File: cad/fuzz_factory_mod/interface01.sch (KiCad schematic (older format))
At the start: 26 parts

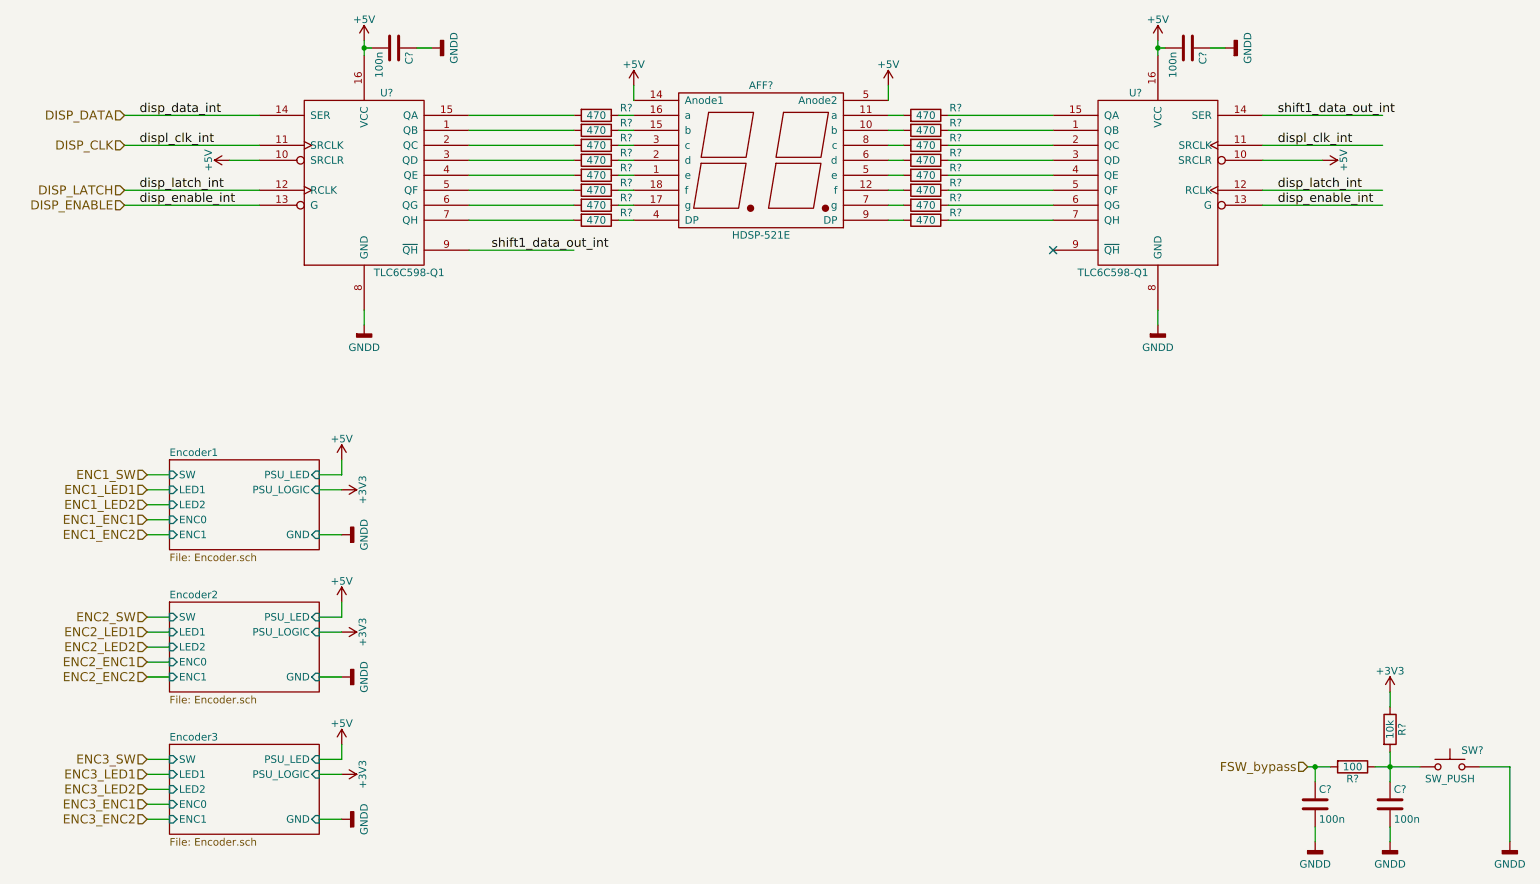
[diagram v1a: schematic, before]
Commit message: Continued schematic.
Modified fuuz_factory circuit : use of matched transistor pairs.
Added USB interface, through FT230X and direct to MCU.
Associated footprints, except for XTAL and trimmers.
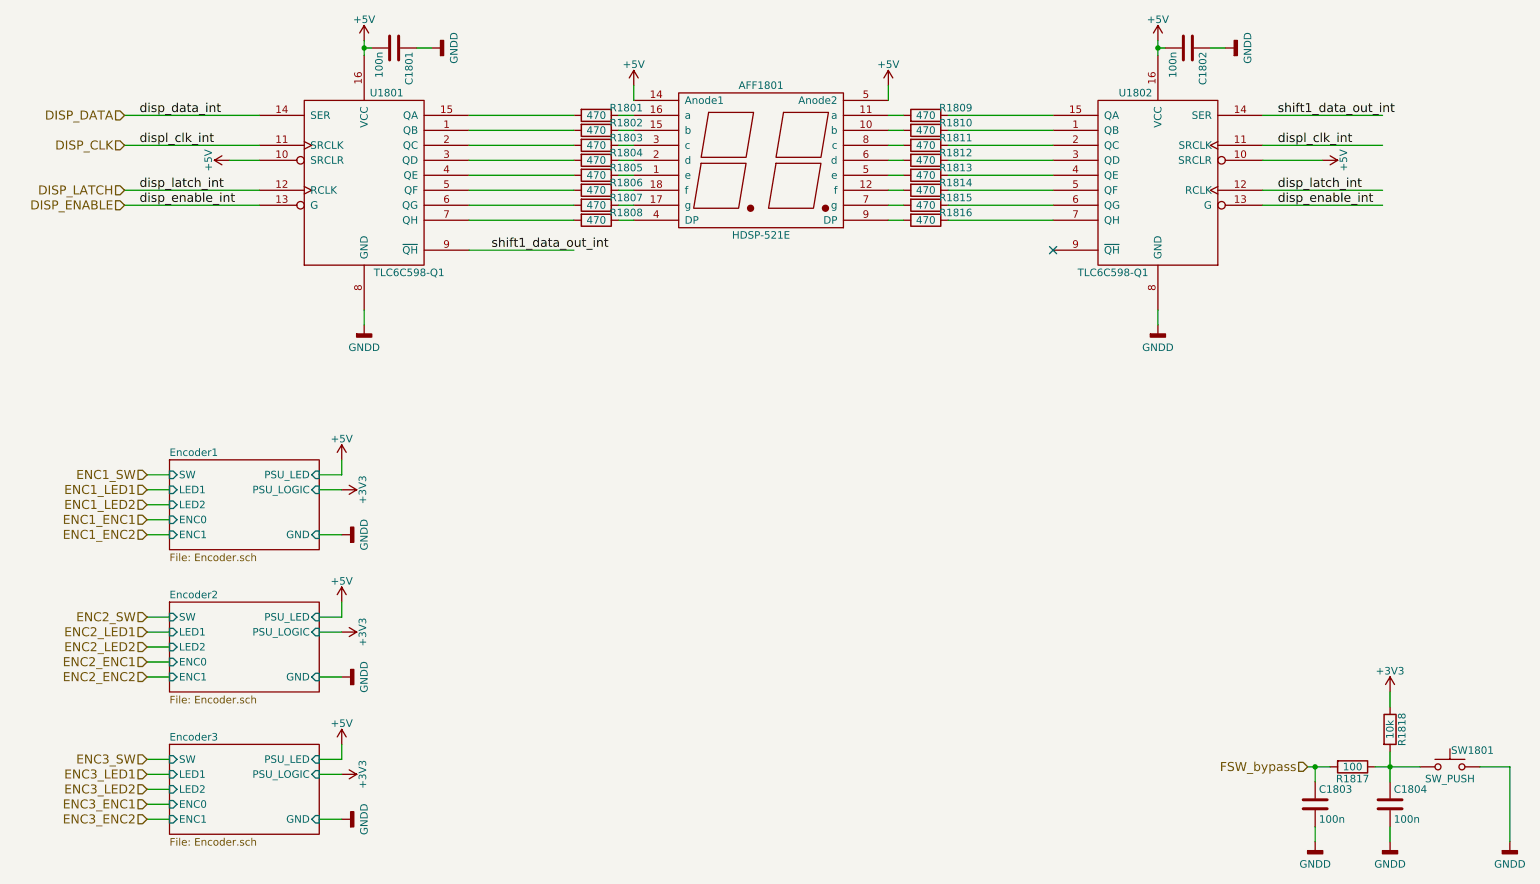
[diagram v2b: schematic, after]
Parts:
- C1801, C1802, C1803, C1804: renamed from C?; footprint Capacitors_SMD:C_0805_HandSoldering -> Capacitors_SMD:C_0603
- R1801, R1802, R1803, R1804, R1805, R1806, R1807, R1808, R1809, R1810, R1811, R1812, R1813, R1814, R1815, R1816: renamed from R?; footprint Resistors_SMD:R_0603_HandSoldering -> Resistors_SMD:R_0805
- R1817, R1818: renamed from R?; footprint Resistors_SMD:R_0603_HandSoldering -> Resistors_SMD:R_0603
- gave numbers to parts that had none: 4
